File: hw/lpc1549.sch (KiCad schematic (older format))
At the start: 16 parts, among them J401 ARM_JTAG_SWD_HEADER_10_PINSMD, U401 LPC1549JBD64, X401 XTAL_7A-12.000MAAJ-T, X402 XTAL_ABS25-32.768KHZ-T

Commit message: 1.7.0 pcb created, not yet ordered
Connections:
- net FLASH_CLK: now also U401.P$8 (PIO0_4/ADC0_4); no longer U401.P$62 (PIO0_27/ACMP_I1)
- net FLASH_CS: now also U401.P$5 (PIO0_1/ADC0_7/SCT0_OUT4); no longer U401.P$61 (PIO0_26/ACMP0_I3/SCT3_OUT3)
- net FLASH_MISO: now also U401.P$6 (PIO0_2/ADC0_6/SCT1_OUT3); no longer U401.P$63 (PIO0_28/ACMP1_I3)
- net FLASH_MOSI: now also U401.P$7 (PIO0_3/ADC0_5/SCT1_OUT4); no longer U401.P$1 (PIO0_30/ADC0_11)
- net LCD_CS: now also U401.P$53 (PIO1_8/ACMP3_I3/SCT3_OUT4); no longer U401.P$38 (PIO1_11/ISP1/USB_VBUS)
- net LCD_MISO: now also U401.P$61 (PIO0_26/ACMP0_I3/SCT3_OUT3); no longer U401.P$53 (PIO1_8/ACMP3_I3/SCT3_OUT4)
- net LCD_MOSI: now also U401.P$58 (PIO0_24/SCT0_OUT6); no longer U401.P$51 (PIO1_7/ADCMP3_I4)
- net LCD_PD: now also U401.P$51 (PIO1_7/ADCMP3_I4); no longer U401.P$54 (PIO1_9/ACMP2_I4/ISP0)
- net LCD_SCK: now also U401.P$62 (PIO0_27/ACMP_I1); no longer U401.P$58 (PIO0_24/SCT0_OUT6)
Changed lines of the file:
@@
 $EndDescr
 $Comp
-L +3V3 #PWR401
+L +3V3 #PWR023
 U 1 1 58FC1E6A
 P 4100 3150
-F 0 "#PWR401" H 4100 3000 50  0001 C CNN
+F 0 "#PWR023" H 4100 3000 50  0001 C CNN
 F 1 "+3V3" H 4115 3323 50  0000 C CNN
 F 2 "" H 4100 3150 50  0000 C CNN
@@
 $EndComp
 $Comp
-L GND #PWR402
+L GND #PWR024
 U 1 1 58FC23D4
 P 4100 4300
-F 0 "#PWR402" H 4100 4050 50  0001 C CNN
+F 0 "#PWR024" H 4100 4050 50  0001 C CNN
 F 1 "GND" H 4105 4127 50  0000 C CNN
 F 2 "" H 4100 4300 50  0000 C CNN
@@
 Text HLabel 6550 5000 2    60   Output ~ 0
 CAN_TX
-Text HLabel 6550 4600 2    60   Input ~ 0
+Text HLabel 6550 5200 2    60   Input ~ 0
 LCD_MISO
+Text HLabel 6550 4700 2    60   Output ~ 0
+LCD_MOSI
+Text HLabel 6550 5300 2    60   Output ~ 0
+LCD_SCK
 Text HLabel 6550 4500 2    60   Output ~ 0
-LCD_MOSI
-Text HLabel 6550 4700 2    60   Output ~ 0
-LCD_SCK
-Text HLabel 6550 4300 2    60   Output ~ 0
 LCD_PD
-Text HLabel 6550 4400 2    60   Output ~ 0
+Text HLabel 6550 4600 2    60   Output ~ 0
 LCD_CS
 $Comp
@@
 $EndComp
 $Comp
-L GND #PWR405
+L GND #PWR025
 U 1 1 5902271B
 P 7850 2750
-F 0 "#PWR405" H 7850 2500 50  0001 C CNN
+F 0 "#PWR025" H 7850 2500 50  0001 C CNN
 F 1 "GND" H 7855 2577 50  0000 C CNN
 F 2 "" H 7850 2750 50  0000 C CNN
@@
 $EndComp
 $Comp
-L +3V3 #PWR407
+L +3V3 #PWR026
 U 1 1 59058BEB
 P 8900 3150
-F 0 "#PWR407" H 8900 3000 50  0001 C CNN
+F 0 "#PWR026" H 8900 3000 50  0001 C CNN
 F 1 "+3V3" H 8915 3323 50  0000 C CNN
 F 2 "" H 8900 3150 50  0000 C CNN
@@
 $EndComp
 $Comp
-L GND #PWR406
+L GND #PWR027
 U 1 1 59058D57
 P 8750 4200
-F 0 "#PWR406" H 8750 3950 50  0001 C CNN
+F 0 "#PWR027" H 8750 3950 50  0001 C CNN
 F 1 "GND" H 8755 4027 50  0000 C CNN
 F 2 "" H 8750 4200 50  0000 C CNN
@@
 	0    1    1    0
 $EndComp
-Text HLabel 6550 5200 2    60   Output ~ 0
+Text HLabel 4150 2300 0    60   Output ~ 0
 FLASH_CS
-Text HLabel 6550 5400 2    60   Input ~ 0
+Text HLabel 4150 2400 0    60   Input ~ 0
 FLASH_MISO
-Text HLabel 4150 1900 0    60   Output ~ 0
+Text HLabel 4150 2500 0    60   Output ~ 0
 FLASH_MOSI
-Text HLabel 6550 5300 2    60   Output ~ 0
+Text HLabel 4150 2600 0    60   Output ~ 0
 FLASH_CLK
 $Comp
@@
 $EndComp
 $Comp
-L GND #PWR403
+L GND #PWR028
 U 1 1 59C7ED66
 P 7550 3450
-F 0 "#PWR403" H 7550 3200 50  0001 C CNN
+F 0 "#PWR028" H 7550 3200 50  0001 C CNN
 F 1 "GND" H 7555 3277 50  0000 C CNN
 F 2 "" H 7550 3450 50  0000 C CNN
@@
 $EndComp
 $Comp
-L GND #PWR404
+L GND #PWR029
 U 1 1 59C7EFA3
 P 7750 3450
-F 0 "#PWR404" H 7750 3200 50  0001 C CNN
+F 0 "#PWR029" H 7750 3200 50  0001 C CNN
 F 1 "GND" H 7755 3277 50  0000 C CNN
 F 2 "" H 7750 3450 50  0000 C CNN
@@
 	6250 4900 6550 4900
 Wire Wire Line
+	6250 5200 6550 5200
+Wire Wire Line
+	6250 4700 6550 4700
+Wire Wire Line
+	6250 5300 6550 5300
+Wire Wire Line
 	6250 4600 6550 4600
 Wire Wire Line
 	6250 4500 6550 4500
-Wire Wire Line
-	6250 4700 6550 4700
-Wire Wire Line
-	6250 4400 6550 4400
-Wire Wire Line
-	6250 4300 6550 4300
 Wire Wire Line
 	6250 2700 7150 2700
@@
 	4350 1700 4450 1700
 Wire Wire Line
-	6250 5200 6550 5200
-Wire Wire Line
-	6250 5400 6550 5400
-Wire Wire Line
-	4150 1900 4450 1900
-Wire Wire Line
-	6250 5300 6550 5300
+	4450 2300 4150 2300
+Wire Wire Line
+	4450 2400 4150 2400
+Wire Wire Line
+	4150 2500 4450 2500
+Wire Wire Line
+	4450 2600 4150 2600
 Wire Wire Line
 	6250 3100 7200 3100

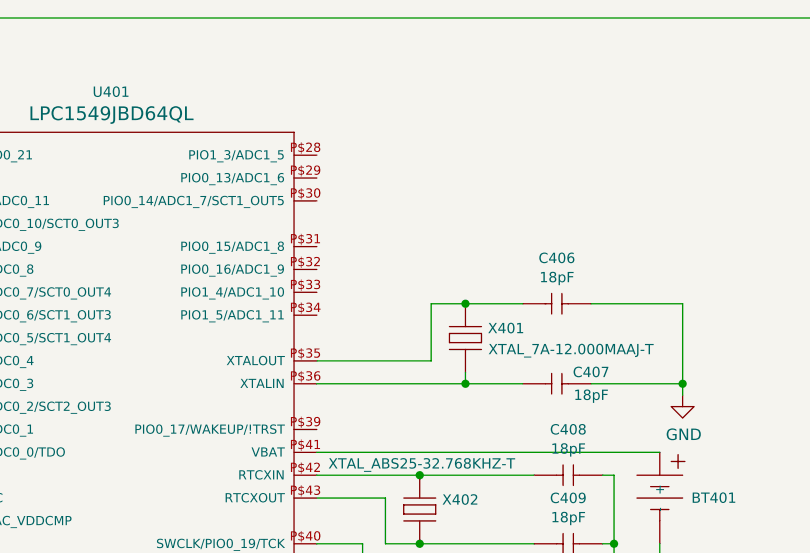
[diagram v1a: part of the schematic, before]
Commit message: uw180s grab times adjustable
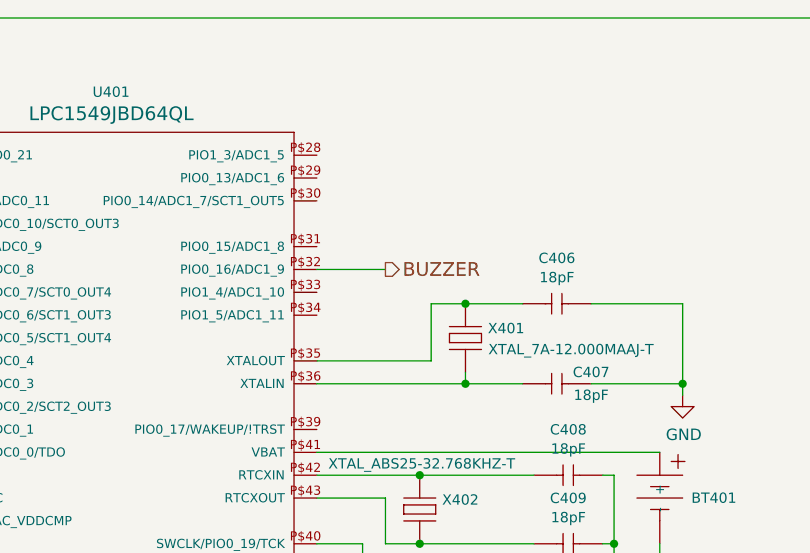
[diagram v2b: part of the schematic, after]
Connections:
- net BUZZER: now reaches U401.P$32 (PIO0_16/ADC1_9)
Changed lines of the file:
@@
 $Descr A4 11693 8268
 encoding utf-8
-Sheet 4 5
+Sheet 4 6
 Title ""
 Date ""
@@
 Wire Wire Line
 	6350 3500 6250 3500
+Wire Wire Line
+	6250 2200 6550 2200
+Text HLabel 6550 2200 2    60   Output ~ 0
+BUZZER
 $EndSCHEMATC
